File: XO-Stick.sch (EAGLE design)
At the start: 29 parts, among them J1 POWER, SW1 USER, U1 TINY85P, U2 TINY861A, U3 ARDUINO-SHIELD, X1 USBPCB, X2 USBMINIB

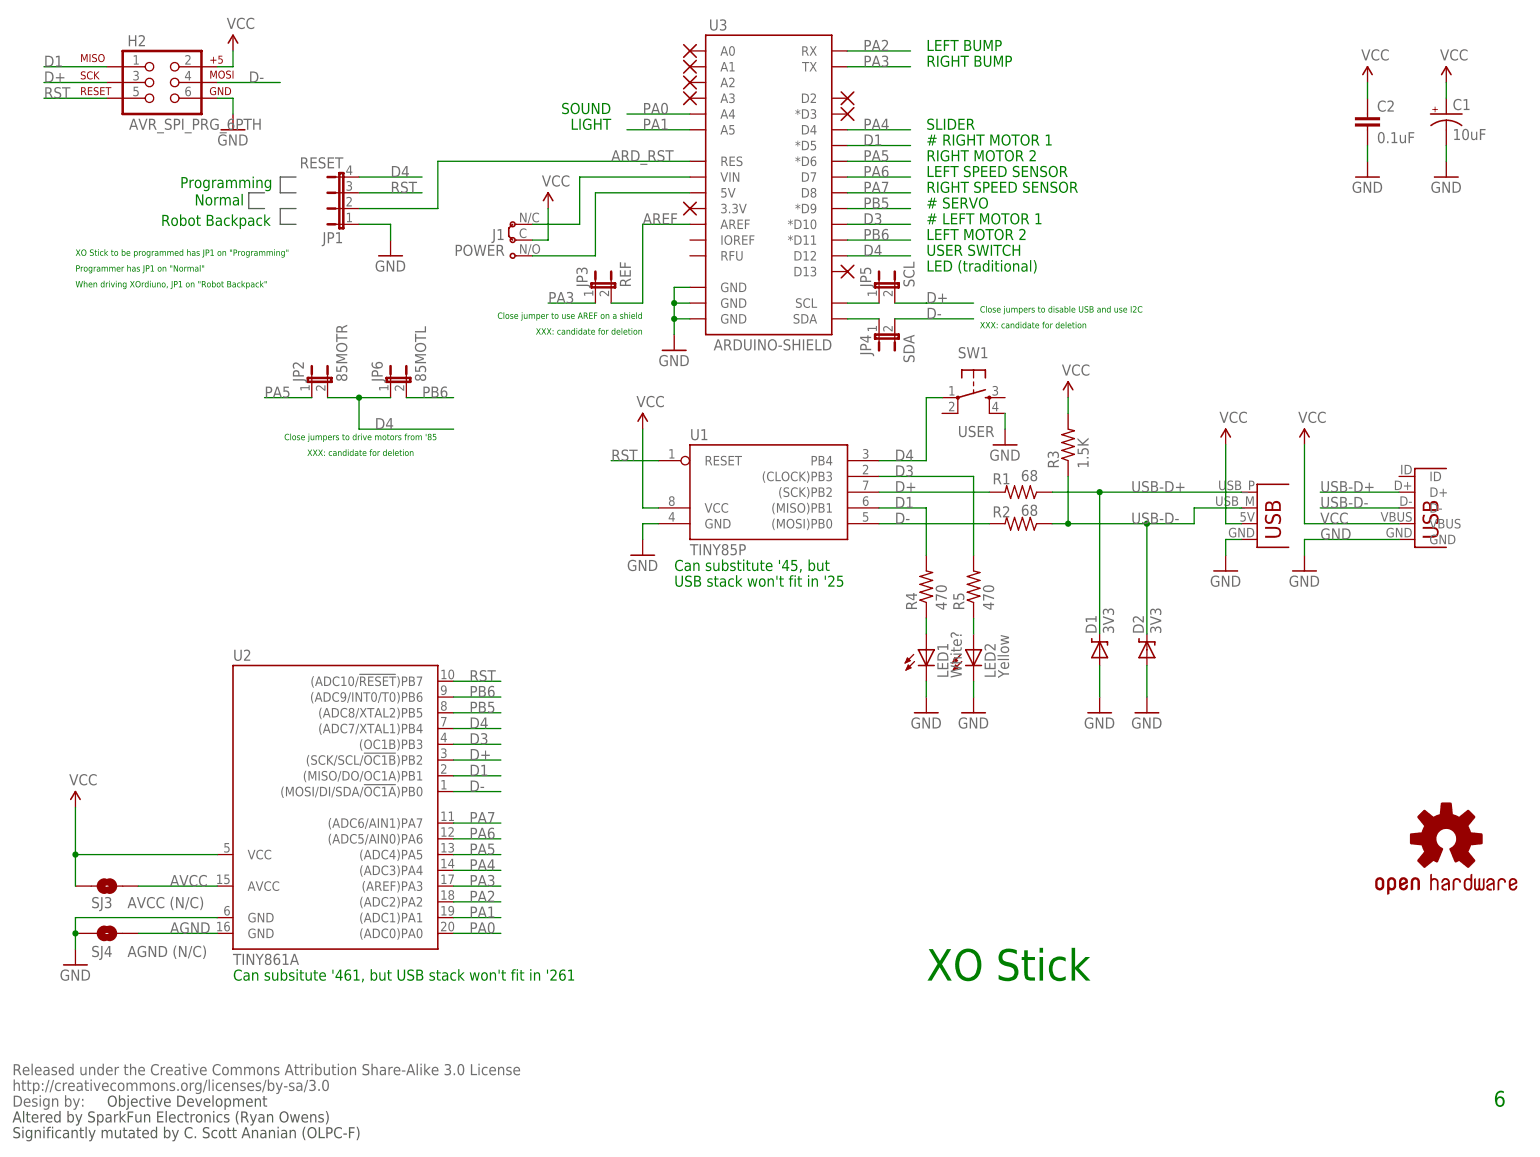
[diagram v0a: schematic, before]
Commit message: v7 of board/schematic.  Fixed remaining issues with v6. 2-layer routing.
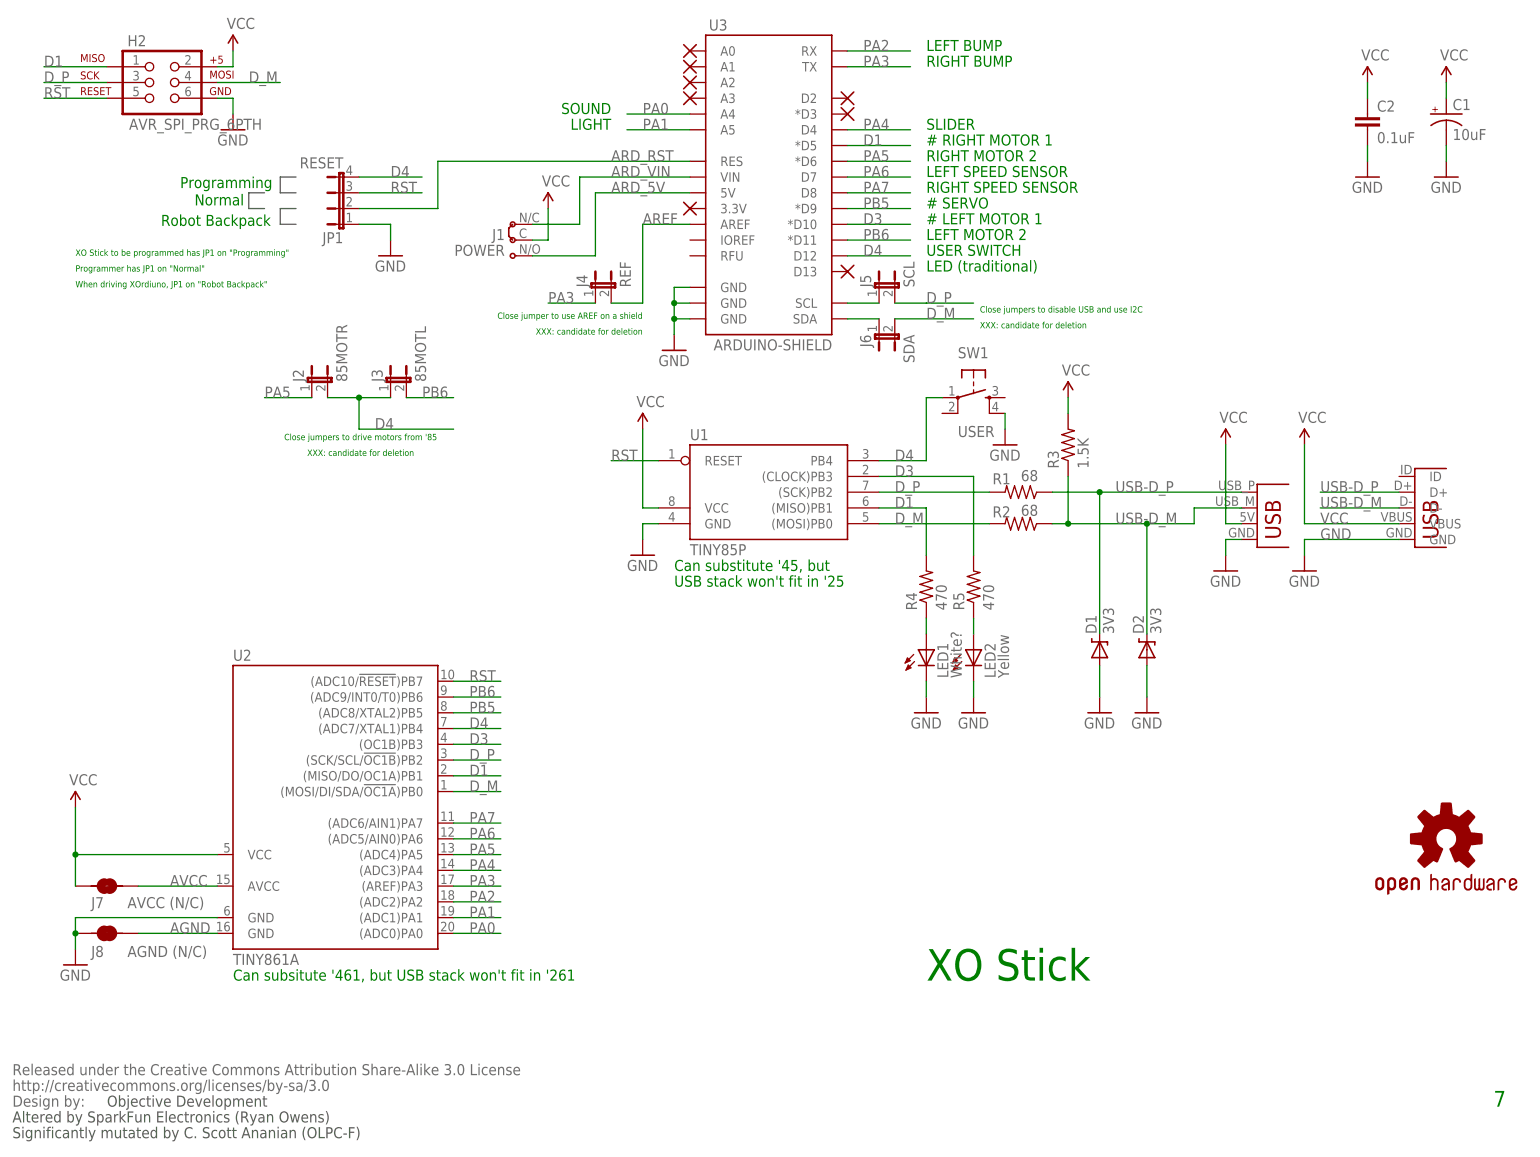
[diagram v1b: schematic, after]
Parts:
- removed JP2: 85MOTR, jumper:JP1E
- removed JP3: REF, jumper:JP1E
- removed JP4: SDA, jumper:JP1E
- removed JP5: SCL, jumper:JP1E
- removed JP6: 85MOTL, jumper:JP1E
- removed SJ3: AVCC (N/C), SparkFun:SOLDERJUMPERTRACE
- removed SJ4: AGND (N/C), SparkFun:SOLDERJUMPERTRACE
- added J2: 85MOTR, xorduino:JUMPER-2SJ-NO
- added J3: 85MOTL, xorduino:JUMPER-2SJ-NO
- added J4: REF, xorduino:JUMPER-2SJ-NO
- added J5: SCL, xorduino:JUMPER-2SJ-NO
- added J6: SDA, xorduino:JUMPER-2SJ-NO
- added J7: AVCC (N/C), xorduino:SOLDERJUMPERBOT-NOCONFLICT
- added J8: AGND (N/C), xorduino:SOLDERJUMPERBOT-NOCONFLICT
- C2: device SparkFun:CAPPTH -> SparkFun-Passives:CAPKIT
- JP1: device jumper:JP4E -> xorduino:JUMPER-4
- LED1, LED2: device SparkFun:LED3MM -> xorduino:LED3MM-KIT
- R1, R2, R3, R4, R5: device SparkFun:RESISTORAXIAL-0.3 -> SparkFun-Passives:RESISTORKIT
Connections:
- net N$1 renamed ARD_VIN
- net N$2 renamed ARD_5V
- net USB-D+ renamed USB-D_P
- net USB-D- renamed USB-D_M
- removed net D+: H2.3, JP5.2, R1.2, U1.(SCK)PB2, U2.(SCK/SCL/!OC1B!)PB2
- removed net D-: H2.4, JP4.2, R2.2, U1.(MOSI)PB0, U2.(MOSI/DI/SDA/!OC1A!)PB0
- new net D_M: H2.4, J6.2, R2.2, U1.(MOSI)PB0, U2.(MOSI/DI/SDA/!OC1A!)PB0
- new net D_P: H2.3, J5.2, R1.2, U1.(SCK)PB2, U2.(SCK/SCL/!OC1B!)PB2
- net AGND: now also J8.2; no longer SJ4.2
- net AREF: now also J4.2; no longer JP3.2
- net AVCC: now also J7.2; no longer SJ3.2
- net D4: now also J2.2, J3.1; no longer JP2.2, JP6.1
- net GND: now also J8.1; no longer SJ4.1
- net PA3: now also J4.1; no longer JP3.1
- net PA5: now also J2.1; no longer JP2.1
- net PB6: now also J3.2; no longer JP6.2
- net SCL: now also J5.1; no longer JP5.1
- net SDA: now also J6.1; no longer JP4.1
- net VCC: now also J7.1; no longer SJ3.1
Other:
- note added: "7"
- note removed: "6"

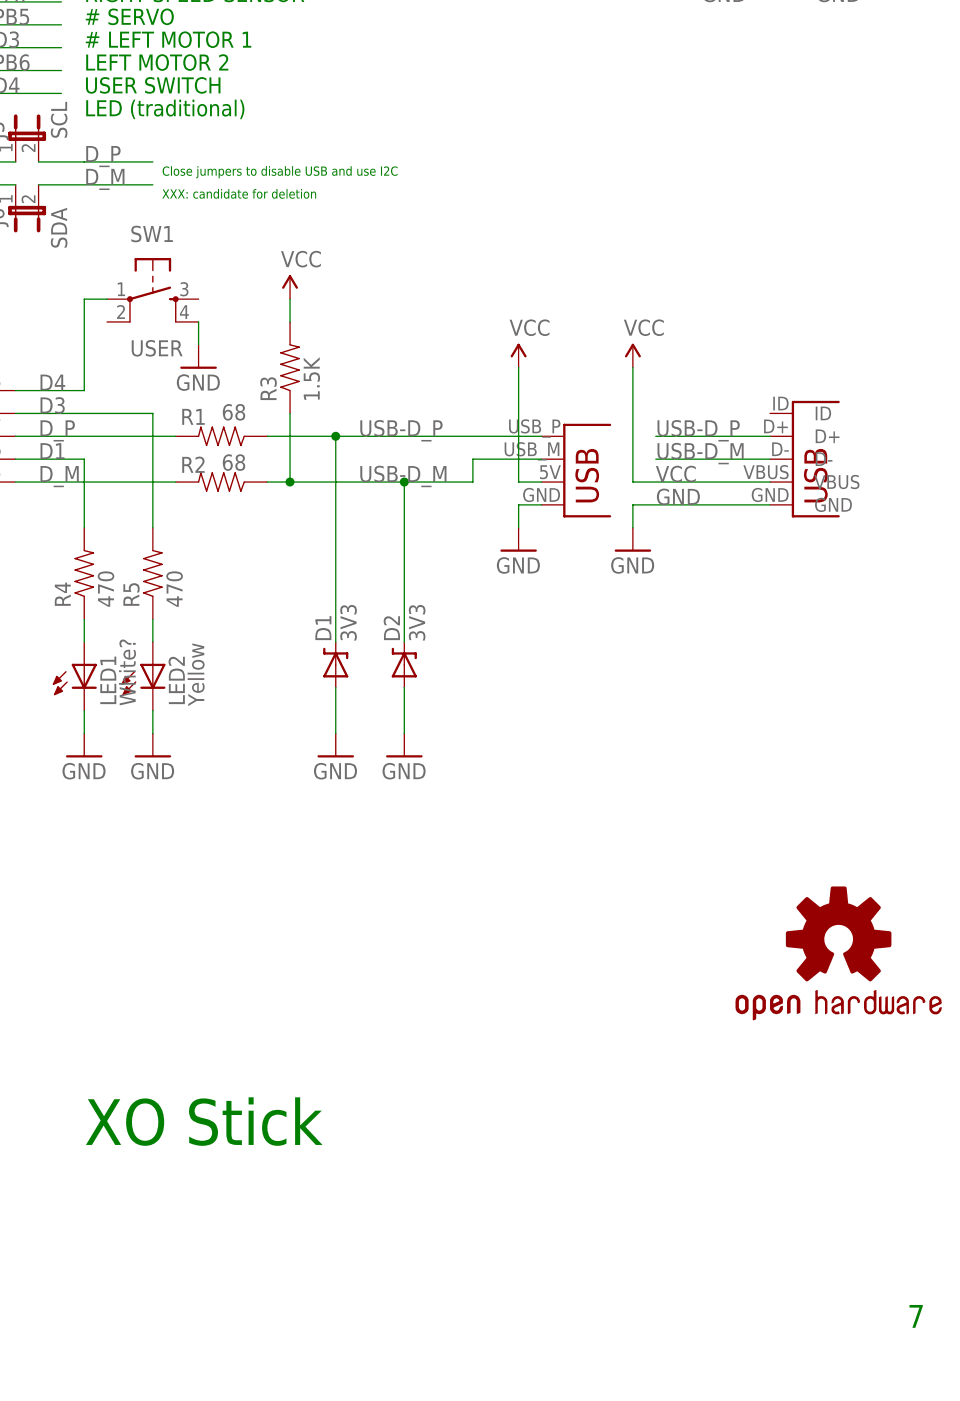
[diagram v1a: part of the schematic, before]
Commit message: XO Stick v8: add jumper between VBUS and VCC; make SDA/SCL jumpers N/C.
SDA and SCL jumpers need to be closed in order to program XO Stick from
an XOrduino. Splitting VBUS from VCC is needed in order to make a 3.3v
variant XO Stick for XO unbricking.
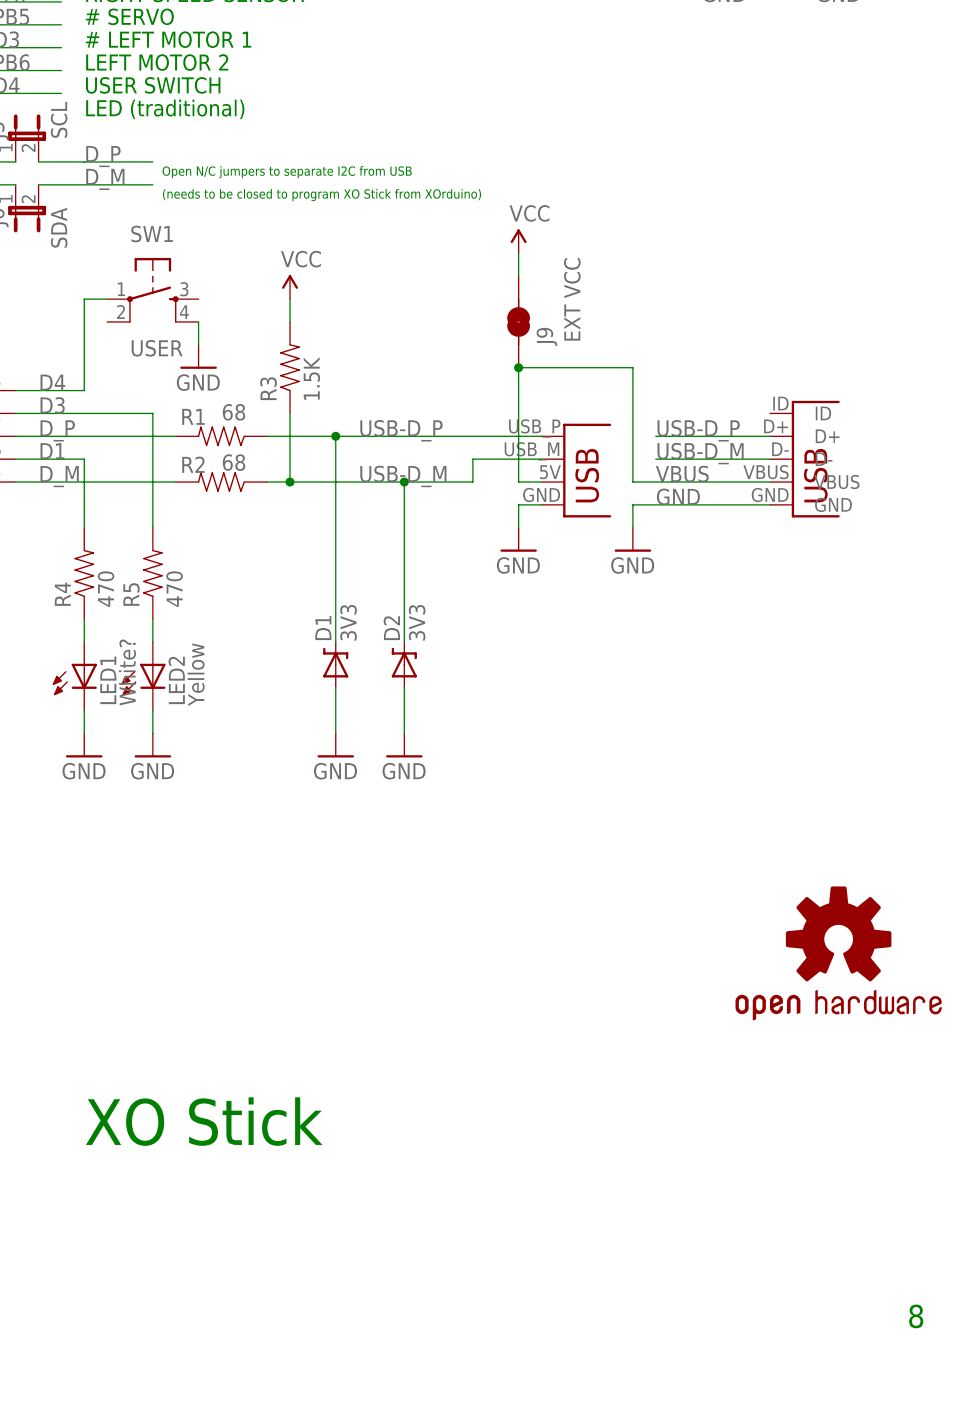
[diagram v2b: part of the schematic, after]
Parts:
- added J9: EXT VCC, xorduino:SOLDERJUMPERBOT-NOCONFLICT-PAD
- J5, J6: device xorduino:JUMPER-2SJ-NO -> xorduino:JUMPER-2SJ-NC-BOT
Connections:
- new net VBUS: J9.1, X1.VBUS, X2.VBUS
- net VCC: now also J9.2; no longer X1.VBUS, X2.VBUS
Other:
- note added: "(needs to be closed to program XO Stick from XOrduino)"
- note added: "8"
- note added: "Open N/C jumpers to separate I2C from USB"
- note removed: "7"
- note removed: "Close jumpers to disable USB and use I2C"
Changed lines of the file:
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@@
 <part name="X2" library="xorduino" deviceset="USB" device="MINIB"/>
 <part name="GND11" library="SparkFun-2" deviceset="GND" device=""/>
-<part name="P+8" library="SparkFun" deviceset="VCC" device=""/>
 <part name="D1" library="SparkFun" deviceset="DIODE-ZENER" device="PTH" value="3V3"/>
 <part name="D2" library="SparkFun" deviceset="DIODE-ZENER" device="PTH" value="3V3"/>
@@
 <part name="J3" library="xorduino" deviceset="JUMPER-2" device="SJ-NO" value="85MOTL"/>
 <part name="J4" library="xorduino" deviceset="JUMPER-2" device="SJ-NO" value="REF"/>
-<part name="J5" library="xorduino" deviceset="JUMPER-2" device="SJ-NO" value="SCL"/>
-<part name="J6" library="xorduino" deviceset="JUMPER-2" device="SJ-NO" value="SDA"/>
+<part name="J5" library="xorduino" deviceset="JUMPER-2" device="SJ-NC-BOT" value="SCL"/>
+<part name="J6" library="xorduino" deviceset="JUMPER-2" device="SJ-NC-BOT" value="SDA"/>
+<part name="J9" library="xorduino" deviceset="SOLDERJUMPER" device="BOT-NOCONFLICT-PAD" value="EXT VCC"/>
 </parts>
 <sheets>
@@
 <text x="2.54" y="5.08" size="1.778" layer="97">Altered by SparkFun Electronics (Ryan Owens)</text>
 <text x="149.86" y="27.94" size="5.08" layer="91">XO Stick</text>
-<text x="241.3" y="7.62" size="2.54" layer="91">7</text>
+<text x="241.3" y="7.62" size="2.54" layer="91">8</text>
 <text x="149.86" y="162.56" size="1.778" layer="91"># RIGHT MOTOR 1</text>
 <text x="149.86" y="152.4" size="1.778" layer="91"># SERVO</text>
@@
 <wire x1="40.64" y1="154.94" x2="43.18" y2="154.94" width="0.1524" layer="97"/>
 <text x="58.674" y="115.062" size="1.016" layer="91" align="bottom-center">Close jumpers to drive motors from '85</text>
-<text x="158.496" y="135.636" size="1.016" layer="91">Close jumpers to disable USB and use I2C</text>
+<text x="158.496" y="135.636" size="1.016" layer="91">Open N/C jumpers to separate I2C from USB</text>
 <text x="12.7" y="144.78" size="1.016" layer="91">XO Stick to be programmed has JP1 on "Programming"</text>
 <text x="12.7" y="142.24" size="1.016" layer="91">Programmer has JP1 on "Normal"</text>
@@
 <text x="58.674" y="112.522" size="1.016" layer="91" align="bottom-center">XXX: candidate for deletion</text>
 <text x="104.14" y="132.08" size="1.016" layer="91" align="bottom-right">XXX: candidate for deletion</text>
-<text x="158.496" y="133.096" size="1.016" layer="91">XXX: candidate for deletion</text>
+<text x="158.496" y="133.096" size="1.016" layer="91">(needs to be closed to program XO Stick from XOrduino)</text>
 <text x="38.1" y="27.94" size="1.778" layer="91">Can subsitute '461, but USB stack won't fit in '261</text>
 <text x="109.22" y="93.98" size="1.778" layer="91">Can substitute '45, but</text>
@@
 <instance part="P+3" gate="1" x="172.72" y="121.92"/>
 <instance part="GND7" gate="1" x="198.12" y="93.98"/>
-<instance part="P+1" gate="1" x="198.12" y="114.3"/>
+<instance part="P+1" gate="1" x="198.12" y="127"/>
 <instance part="R3" gate="G$1" x="172.72" y="114.3" rot="R90"/>
 <instance part="R2" gate="G$1" x="165.1" y="101.6" smashed="yes" rot="R180">
@@
 <instance part="X2" gate="G$1" x="228.6" y="99.06"/>
 <instance part="GND11" gate="1" x="210.82" y="93.98"/>
-<instance part="P+8" gate="1" x="210.82" y="114.3"/>
 <instance part="D1" gate="G$1" x="177.8" y="81.28" rot="R90"/>
 <instance part="D2" gate="G$1" x="185.42" y="81.28" rot="R90"/>
@@
 <instance part="J5" gate="G$1" x="142.24" y="139.7"/>
 <instance part="J6" gate="G$1" x="142.24" y="132.08" rot="MR180"/>
+<instance part="J9" gate="G$1" x="198.12" y="119.38" smashed="yes" rot="R90">
+<attribute name="NAME" x="201.93" y="116.84" size="1.778" layer="95" rot="R90"/>
+<attribute name="VALUE" x="204.978" y="117.094" size="1.778" layer="96" rot="R90"/>
+</instance>
 </instances>
 <busses>
@@
 <pinref part="H2" gate="G$1" pin="2"/>
 <pinref part="P+6" gate="1" pin="VCC"/>
-</segment>
-<segment>
-<wire x1="200.66" y1="101.6" x2="198.12" y2="101.6" width="0.1524" layer="91"/>
-<wire x1="198.12" y1="101.6" x2="198.12" y2="114.3" width="0.1524" layer="91"/>
-<pinref part="X1" gate="G$1" pin="VBUS"/>
-<pinref part="P+1" gate="1" pin="VCC"/>
 </segment>
 <segment>
@@
 </segment>
 <segment>
-<wire x1="226.06" y1="101.6" x2="210.82" y2="101.6" width="0.1524" layer="91"/>
-<wire x1="210.82" y1="101.6" x2="210.82" y2="114.3" width="0.1524" layer="91"/>
-<label x="213.36" y="101.6" size="1.778" layer="95"/>
-<pinref part="X2" gate="G$1" pin="VBUS"/>
-<pinref part="P+8" gate="1" pin="VCC"/>
-</segment>
-<segment>
 <pinref part="P+9" gate="1" pin="VCC"/>
 <pinref part="J1" gate="G$1" pin="C"/>
 <wire x1="88.9" y1="152.4" x2="88.9" y2="147.32" width="0.1524" layer="91"/>
 <wire x1="88.9" y1="147.32" x2="86.36" y2="147.32" width="0.1524" layer="91"/>
+</segment>
+<segment>
+<pinref part="P+1" gate="1" pin="VCC"/>
+<pinref part="J9" gate="G$1" pin="2"/>
+<wire x1="198.12" y1="127" x2="198.12" y2="124.46" width="0.1524" layer="91"/>
 </segment>
 </net>
@@
 </segment>
 </net>
+<net name="VBUS" class="1">
+<segment>
+<wire x1="200.66" y1="101.6" x2="198.12" y2="101.6" width="0.1524" layer="91"/>
+<pinref part="X1" gate="G$1" pin="VBUS"/>
+<pinref part="J9" gate="G$1" pin="1"/>
+<wire x1="198.12" y1="101.6" x2="198.12" y2="114.3" width="0.1524" layer="91"/>
+<wire x1="226.06" y1="101.6" x2="210.82" y2="101.6" width="0.1524" layer="91"/>
+<wire x1="210.82" y1="101.6" x2="210.82" y2="114.3" width="0.1524" layer="91"/>
+<label x="213.36" y="101.6" size="1.778" layer="95"/>
+<pinref part="X2" gate="G$1" pin="VBUS"/>
+<wire x1="198.12" y1="114.3" x2="210.82" y2="114.3" width="0.1524" layer="91"/>
+<junction x="198.12" y="114.3"/>
+</segment>
+</net>

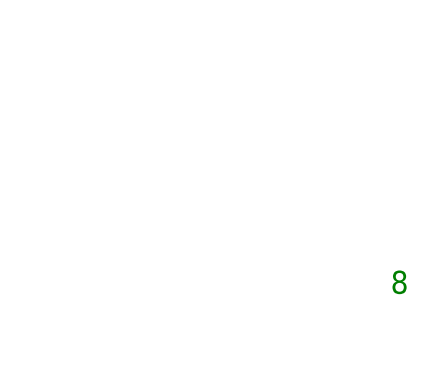
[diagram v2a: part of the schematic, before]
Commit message: XO Stick v9: add silkscreen to break-off tabs, move some traces.
Moved traces away from break-off tabs and removed one trace from the
top side of the USB connector.
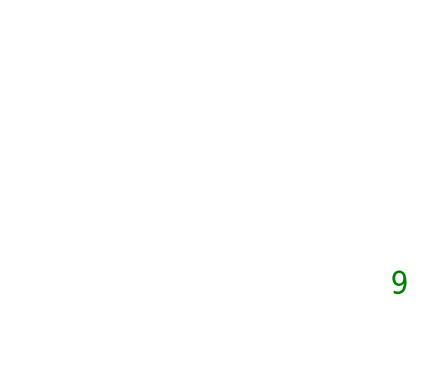
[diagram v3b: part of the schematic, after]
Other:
- note added: "9"
- note removed: "8"
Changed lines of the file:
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@@
 <text x="2.54" y="5.08" size="1.778" layer="97">Altered by SparkFun Electronics (Ryan Owens)</text>
 <text x="149.86" y="27.94" size="5.08" layer="91">XO Stick</text>
-<text x="241.3" y="7.62" size="2.54" layer="91">8</text>
+<text x="241.3" y="7.62" size="2.54" layer="91">9</text>
 <text x="149.86" y="162.56" size="1.778" layer="91"># RIGHT MOTOR 1</text>
 <text x="149.86" y="152.4" size="1.778" layer="91"># SERVO</text>
